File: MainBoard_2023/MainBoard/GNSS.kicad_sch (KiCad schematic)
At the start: 13 parts

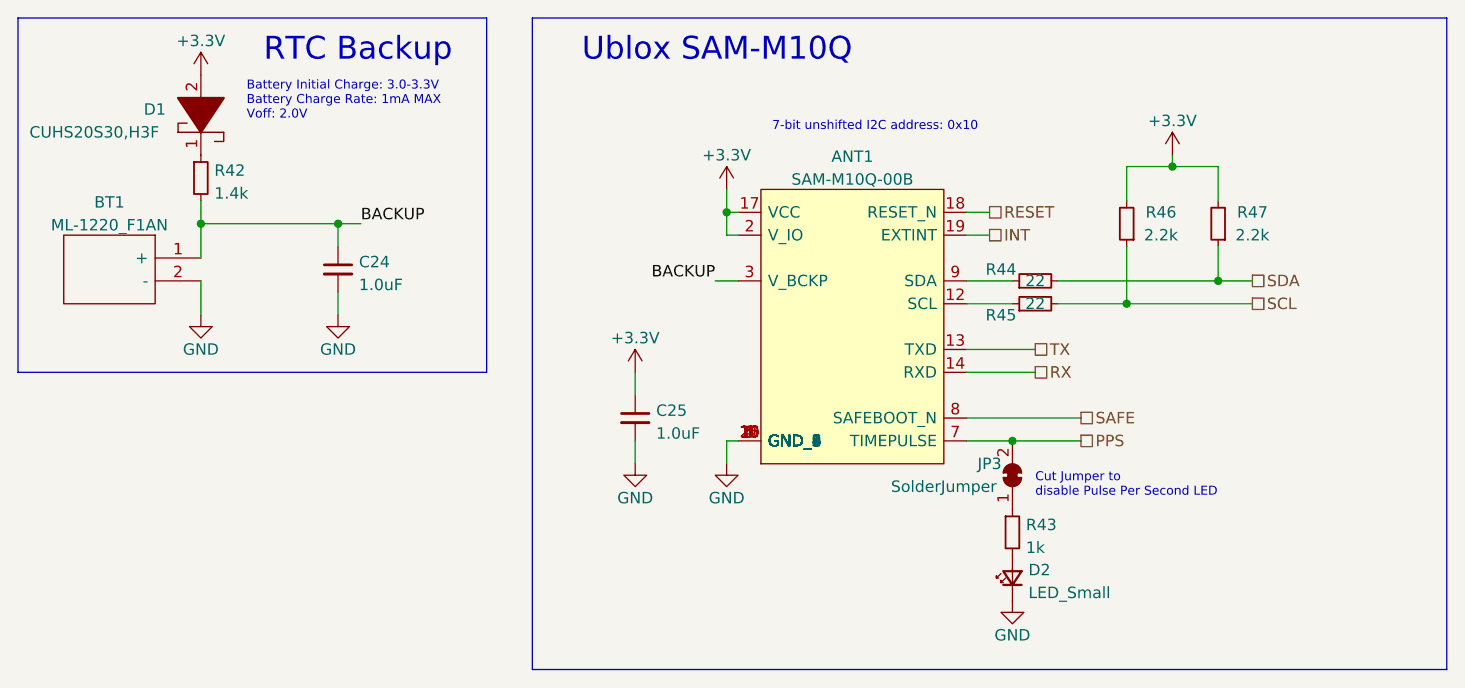
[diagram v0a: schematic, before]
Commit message: シルクを整えた
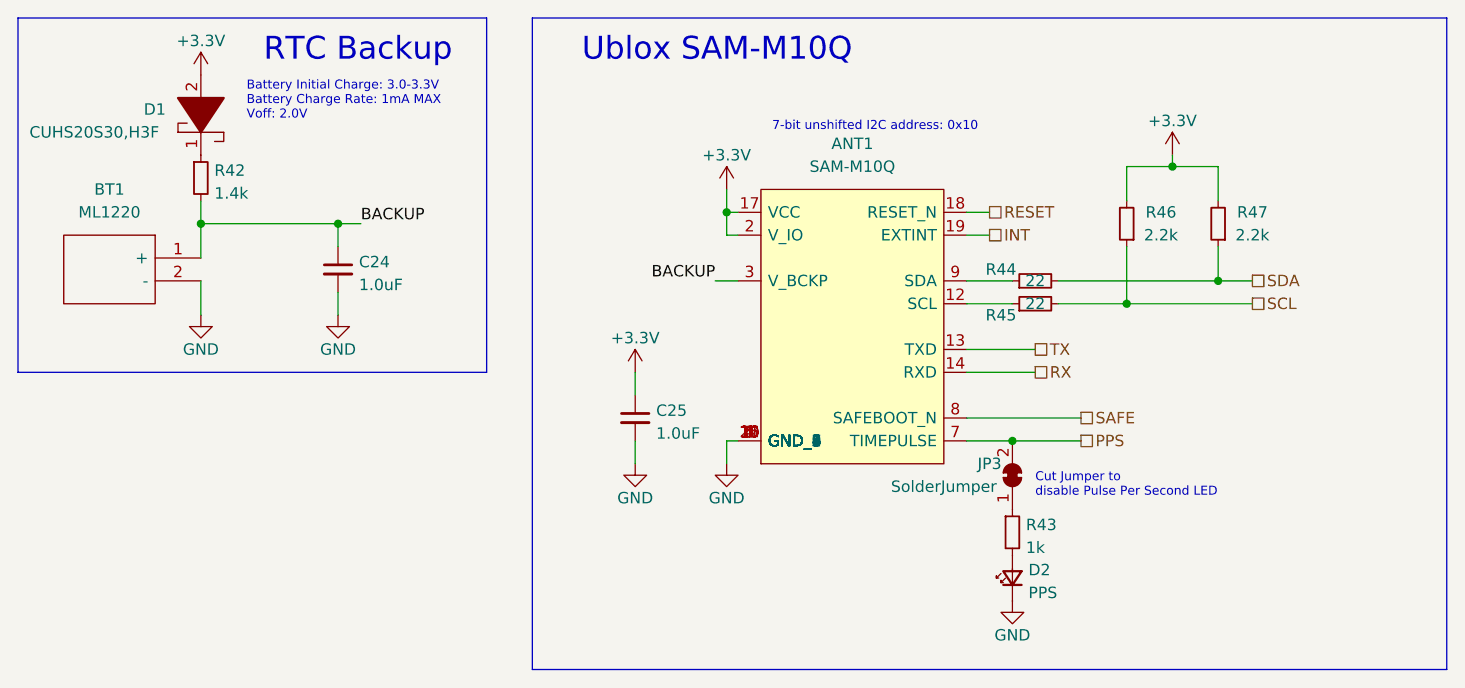
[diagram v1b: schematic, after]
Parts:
- ANT1: value SAM-M10Q-00B -> SAM-M10Q
- BT1: value ML-1220_F1AN -> ML1220
- D2: value LED_Small -> PPS
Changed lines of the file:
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@@
   (symbol (lib_id "ML-1220_F1AN:ML-1220_F1AN") (at 87.63 83.82 0) (mirror y) (unit 1)
     (in_bom yes) (on_board yes) (fields_autoplaced)
-    (property "Reference" "BT1" (id 0) (at 77.47 77.631 0))
-    (property "Value" "ML-1220_F1AN" (id 1) (at 77.47 80.1679 0))
+    (property "Reference" "BT1" (id 0) (at 77.47 76.2 0))
+    (property "Value" "ML1220" (id 1) (at 77.47 78.74 0))
     (property "Footprint" "ML-1220_F1AN:ML-1220_F1AN" (id 2) (at 71.12 81.28 0)
       (effects (font (size 1.27 1.27)) (justify left) hide)
@@
   (symbol (lib_id "SAM-M10Q-00B:SAM-M10Q-00B") (at 160.02 91.44 0) (unit 1)
     (in_bom yes) (on_board yes) (fields_autoplaced)
-    (property "Reference" "ANT1" (id 0) (at 160.02 72.551 0))
-    (property "Value" "SAM-M10Q-00B" (id 1) (at 160.02 75.0879 0))
+    (property "Reference" "ANT1" (id 0) (at 160.02 71.12 0))
+    (property "Value" "SAM-M10Q" (id 1) (at 160.02 73.66 0))
     (property "Footprint" "SAM-M10Q-00B:SAM-M10Q-00B" (id 2) (at 177.8 92.71 0)
       (effects (font (size 1.27 1.27)) (justify left) hide)
@@
       (effects (font (size 1.27 1.27)) (justify right))
     )
-    (property "Value" "LED_Small" (id 1) (at 179.578 121.0187 90)
+    (property "Value" "PPS" (id 1) (at 179.578 121.0187 90)
       (effects (font (size 1.27 1.27)) (justify right))
     )
